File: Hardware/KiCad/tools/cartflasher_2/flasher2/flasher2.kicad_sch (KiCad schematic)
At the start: 30 parts, among them J1 USB_C_Receptacle_USB2.0, J2 ICSP, SW1 SW_Push, U2 AVR64DA64-I/PT, U3 FT232RL

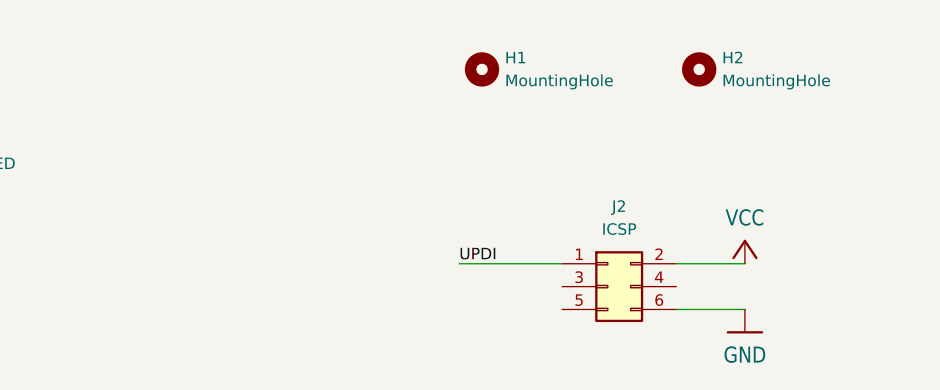
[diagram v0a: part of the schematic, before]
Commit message: flasher2 sent for prototype production
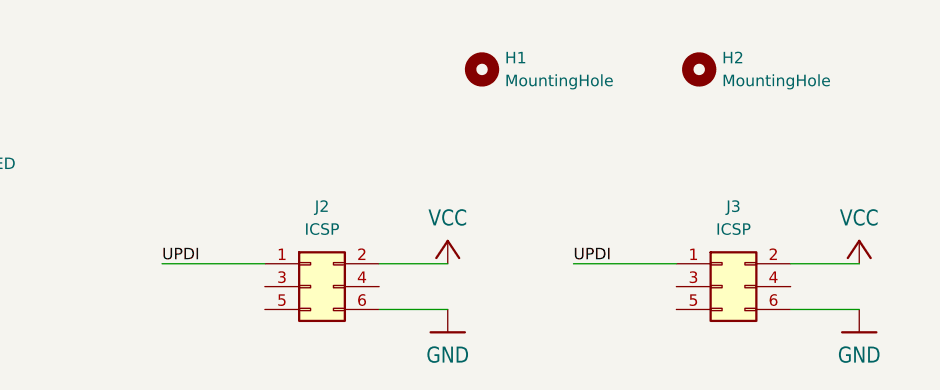
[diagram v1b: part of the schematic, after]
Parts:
- added J3: ICSP, Connector:Tag-Connect_TC2030-IDC-FP_2x03_P1.27mm_Vertical, symbol Connector_Generic:Conn_02x03_Odd_Even
- U2: MPN (none) -> AVR64DA64-I/PT
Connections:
- net GND: now also J3.6 (Pin_6)
- net UPDI: now also J3.1 (Pin_1)
- net VCC: now also J3.2 (Pin_2)
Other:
- moved on the sheet: J2
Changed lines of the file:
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@@
+    (stroke (width 0) (type default))
+  )
+  (wire (pts (xy 280.67 199.39) (xy 288.29 199.39))
     (stroke (width 0) (type default))
   )
@@
     (stroke (width 0) (type default))
   )
+  (wire (pts (xy 256.54 194.31) (xy 267.97 194.31))
+    (stroke (width 0) (type default))
+  )
   (wire (pts (xy 179.07 109.22) (xy 196.85 109.22))
     (stroke (width 0) (type default))
@@
     (stroke (width 0.1524) (type solid))
   )
-  (wire (pts (xy 243.84 194.31) (xy 255.27 194.31))
+  (wire (pts (xy 210.82 194.31) (xy 222.25 194.31))
     (stroke (width 0) (type default))
   )
@@
     (stroke (width 0) (type default))
   )
+  (wire (pts (xy 280.67 194.31) (xy 288.29 194.31))
+    (stroke (width 0) (type default))
+  )
   (wire (pts (xy 119.38 80.01) (xy 129.54 80.01))
     (stroke (width 0) (type default))
@@
     (stroke (width 0) (type default))
   )
-  (wire (pts (xy 267.97 194.31) (xy 275.59 194.31))
+  (wire (pts (xy 234.95 194.31) (xy 242.57 194.31))
     (stroke (width 0) (type default))
   )
@@
     (stroke (width 0) (type default))
   )
-  (wire (pts (xy 267.97 199.39) (xy 275.59 199.39))
+  (wire (pts (xy 234.95 199.39) (xy 242.57 199.39))
     (stroke (width 0) (type default))
   )
@@
     (effects (font (size 1.27 1.27)) (justify left bottom))
   )
+  (label "UPDI" (at 256.54 194.31 0) (fields_autoplaced)
+    (effects (font (size 1.27 1.27)) (justify left bottom))
+  )
   (label "D3" (at 73.66 38.1 0) (fields_autoplaced)
     (effects (font (size 1.2446 1.2446)) (justify left bottom))
@@
     (effects (font (size 1.27 1.27)) (justify left bottom))
   )
-  (label "UPDI" (at 243.84 194.31 0) (fields_autoplaced)
+  (label "UPDI" (at 210.82 194.31 0) (fields_autoplaced)
     (effects (font (size 1.27 1.27)) (justify left bottom))
   )
@@
     )
   )
-  (symbol (lib_id "MegaProgrammer-eagle-import:VCC") (at 275.59 191.77 0) (unit 1)
-    (in_bom yes) (on_board yes) (dnp no) (fields_autoplaced)
-    (property "Reference" "#P+04" (at 275.59 191.77 0)
-      (effects (font (size 1.27 1.27)) hide)
-    )
-    (property "Value" "VCC" (at 275.59 189.23 0)
+  (symbol (lib_id "MegaProgrammer-eagle-import:VCC") (at 242.57 191.77 0) (unit 1)
+    (in_bom yes) (on_board yes) (dnp no) (fields_autoplaced)
+    (property "Reference" "#P+04" (at 242.57 191.77 0)
+      (effects (font (size 1.27 1.27)) hide)
+    )
+    (property "Value" "VCC" (at 242.57 189.23 0)
       (effects (font (size 1.778 1.5113)))
     )
-    (property "Footprint" "" (at 275.59 191.77 0)
-      (effects (font (size 1.27 1.27)) hide)
-    )
-    (property "Datasheet" "" (at 275.59 191.77 0)
+    (property "Footprint" "" (at 242.57 191.77 0)
+      (effects (font (size 1.27 1.27)) hide)
+    )
+    (property "Datasheet" "" (at 242.57 191.77 0)
       (effects (font (size 1.27 1.27)) hide)
     )
@@
     )
   )
+  (symbol (lib_id "Connector_Generic:Conn_02x03_Odd_Even") (at 273.05 196.85 0) (unit 1)
+    (in_bom yes) (on_board yes) (dnp no) (fields_autoplaced)
+    (property "Reference" "J3" (at 274.32 187.96 0)
+      (effects (font (size 1.27 1.27)))
+    )
+    (property "Value" "ICSP" (at 274.32 190.5 0)
+      (effects (font (size 1.27 1.27)))
+    )
+    (property "Footprint" "Connector:Tag-Connect_TC2030-IDC-FP_2x03_P1.27mm_Vertical" (at 273.05 196.85 0)
+      (effects (font (size 1.27 1.27)) hide)
+    )
+    (property "Datasheet" "~" (at 273.05 196.85 0)
+      (effects (font (size 1.27 1.27)) hide)
+    )
+    (property "MPN" "M20-8760342" (at 273.05 196.85 0)
+      (effects (font (size 1.27 1.27)) hide)
+    )
+    (pin "1")
+    (pin "2")
+    (pin "3")
+    (pin "4")
+    (pin "5")
+    (pin "6")
+    (instances
+      (project "flasher2"
+        (path "/28b5c39a-3bca-4ae3-9c02-98d1dbafe5a4"
+          (reference "J3") (unit 1)
+        )
+      )
+    )
+  )
   (symbol (lib_id "Device:R") (at 66.04 139.7 0) (unit 1)
     (in_bom yes) (on_board yes) (dnp no) (fields_autoplaced)
@@
     )
   )
-  (symbol (lib_id "MegaProgrammer-eagle-import:GND") (at 275.59 201.93 0) (unit 1)
-    (in_bom yes) (on_board yes) (dnp no) (fields_autoplaced)
-    (property "Reference" "#GND05" (at 275.59 201.93 0)
-      (effects (font (size 1.27 1.27)) hide)
-    )
-    (property "Value" "GND" (at 275.59 204.47 0)
+  (symbol (lib_id "MegaProgrammer-eagle-import:GND") (at 242.57 201.93 0) (unit 1)
+    (in_bom yes) (on_board yes) (dnp no) (fields_autoplaced)
+    (property "Reference" "#GND05" (at 242.57 201.93 0)
+      (effects (font (size 1.27 1.27)) hide)
+    )
+    (property "Value" "GND" (at 242.57 204.47 0)
       (effects (font (size 1.778 1.5113)))
     )
-    (property "Footprint" "" (at 275.59 201.93 0)
-      (effects (font (size 1.27 1.27)) hide)
-    )
-    (property "Datasheet" "" (at 275.59 201.93 0)
+    (property "Footprint" "" (at 242.57 201.93 0)
+      (effects (font (size 1.27 1.27)) hide)
+    )
+    (property "Datasheet" "" (at 242.57 201.93 0)
       (effects (font (size 1.27 1.27)) hide)
     )
@@
     (property "Datasheet" "AVR64DA64-I/PT" (at 227.33 44.45 0)
       (effects (font (size 1.27 1.27) italic) hide)
+    )
+    (property "MPN" "AVR64DA64-I/PT" (at 196.85 45.72 0)
+      (effects (font (size 1.27 1.27)) hide)
     )
     (pin "1")
@@
     )
   )
+  (symbol (lib_id "MegaProgrammer-eagle-import:GND") (at 288.29 201.93 0) (unit 1)
+    (in_bom yes) (on_board yes) (dnp no) (fields_autoplaced)
+    (property "Reference" "#GND06" (at 288.29 201.93 0)
+      (effects (font (size 1.27 1.27)) hide)
+    )
+    (property "Value" "GND" (at 288.29 204.47 0)
+      (effects (font (size 1.778 1.5113)))
+    )
+    (property "Footprint" "" (at 288.29 201.93 0)
+      (effects (font (size 1.27 1.27)) hide)
+    )
+    (property "Datasheet" "" (at 288.29 201.93 0)
+      (effects (font (size 1.27 1.27)) hide)
+    )
+    (pin "1")
+    (instances
+      (project "flasher2"
+        (path "/28b5c39a-3bca-4ae3-9c02-98d1dbafe5a4"
+          (reference "#GND06") (unit 1)
+        )
+      )
+    )
+  )
   (symbol (lib_id "Device:C") (at 153.67 83.82 0) (unit 1)
     (in_bom yes) (on_board yes) (dnp no) (fields_autoplaced)
@@
     )
   )
-  (symbol (lib_id "Connector_Generic:Conn_02x03_Odd_Even") (at 260.35 196.85 0) (unit 1)
-    (in_bom yes) (on_board yes) (dnp no) (fields_autoplaced)
-    (property "Reference" "J2" (at 261.62 187.96 0)
+  (symbol (lib_id "Connector_Generic:Conn_02x03_Odd_Even") (at 227.33 196.85 0) (unit 1)
+    (in_bom yes) (on_board yes) (dnp no) (fields_autoplaced)
+    (property "Reference" "J2" (at 228.6 187.96 0)
       (effects (font (size 1.27 1.27)))
     )
-    (property "Value" "ICSP" (at 261.62 190.5 0)
+    (property "Value" "ICSP" (at 228.6 190.5 0)
       (effects (font (size 1.27 1.27)))
     )
-    (property "Footprint" "Connector_PinHeader_2.54mm:PinHeader_2x03_P2.54mm_Vertical_SMD" (at 260.35 196.85 0)
-      (effects (font (size 1.27 1.27)) hide)
-    )
-    (property "Datasheet" "~" (at 260.35 196.85 0)
-      (effects (font (size 1.27 1.27)) hide)
-    )
-    (property "MPN" "M20-8760342" (at 260.35 196.85 0)
+    (property "Footprint" "Connector_PinHeader_2.54mm:PinHeader_2x03_P2.54mm_Vertical_SMD" (at 227.33 196.85 0)
+      (effects (font (size 1.27 1.27)) hide)
+    )
+    (property "Datasheet" "~" (at 227.33 196.85 0)
+      (effects (font (size 1.27 1.27)) hide)
+    )
+    (property "MPN" "M20-8760342" (at 227.33 196.85 0)
       (effects (font (size 1.27 1.27)) hide)
     )
@@
         )
       )
+    )
+  )
+  (symbol (lib_id "MegaProgrammer-eagle-import:VCC") (at 288.29 191.77 0) (unit 1)
+    (in_bom yes) (on_board yes) (dnp no) (fields_autoplaced)
+    (property "Reference" "#P+05" (at 288.29 191.77 0)
+      (effects (font (size 1.27 1.27)) hide)
+    )
+    (property "Value" "VCC" (at 288.29 189.23 0)
+      (effects (font (size 1.778 1.5113)))
+    )
+    (property "Footprint" "" (at 288.29 191.77 0)
+      (effects (font (size 1.27 1.27)) hide)
+    )
+    (property "Datasheet" "" (at 288.29 191.77 0)
+      (effects (font (size 1.27 1.27)) hide)
+    )
+    (pin "1")
+    (instances
+      (project "flasher2"
+        (path "/28b5c39a-3bca-4ae3-9c02-98d1dbafe5a4"
+          (reference "#P+05") (unit 1)
+        )
+      )
